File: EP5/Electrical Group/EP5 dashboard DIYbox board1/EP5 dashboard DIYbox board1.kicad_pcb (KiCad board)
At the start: 2 copper layers, 138.2 x 72.5 mm, 161 parts, among them J1 pedal2-2, J10 12864, J11 pedal1-1, J12 pedal1-2, J14 screen, J2 pedal2-1, J4 R1, J5 L1, J6 L2, J7 L3, J8 L4, J9 RTD, U1 Seg1, U10 74HC595, U11 74HC595, U12 74HC595, U13 74HC595, U14 74HC595, U15 74HC595, U16 74HC595, U17 74HC595, U2 Seg2, U5 Seg3, U6 Seg4, U7 74HC595, U8 74HC595, U9 74HC595

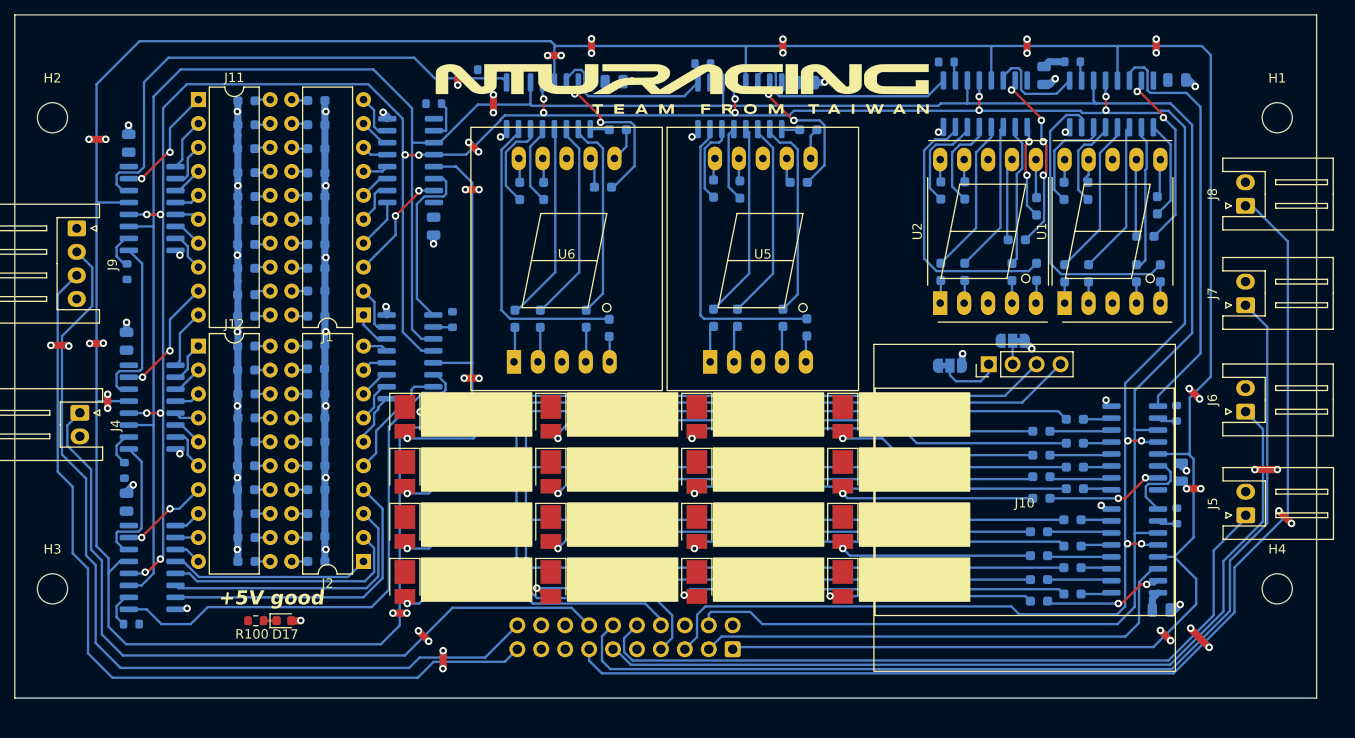
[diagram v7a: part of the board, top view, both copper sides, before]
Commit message: update dashboard 1 to V2.3 in EP5
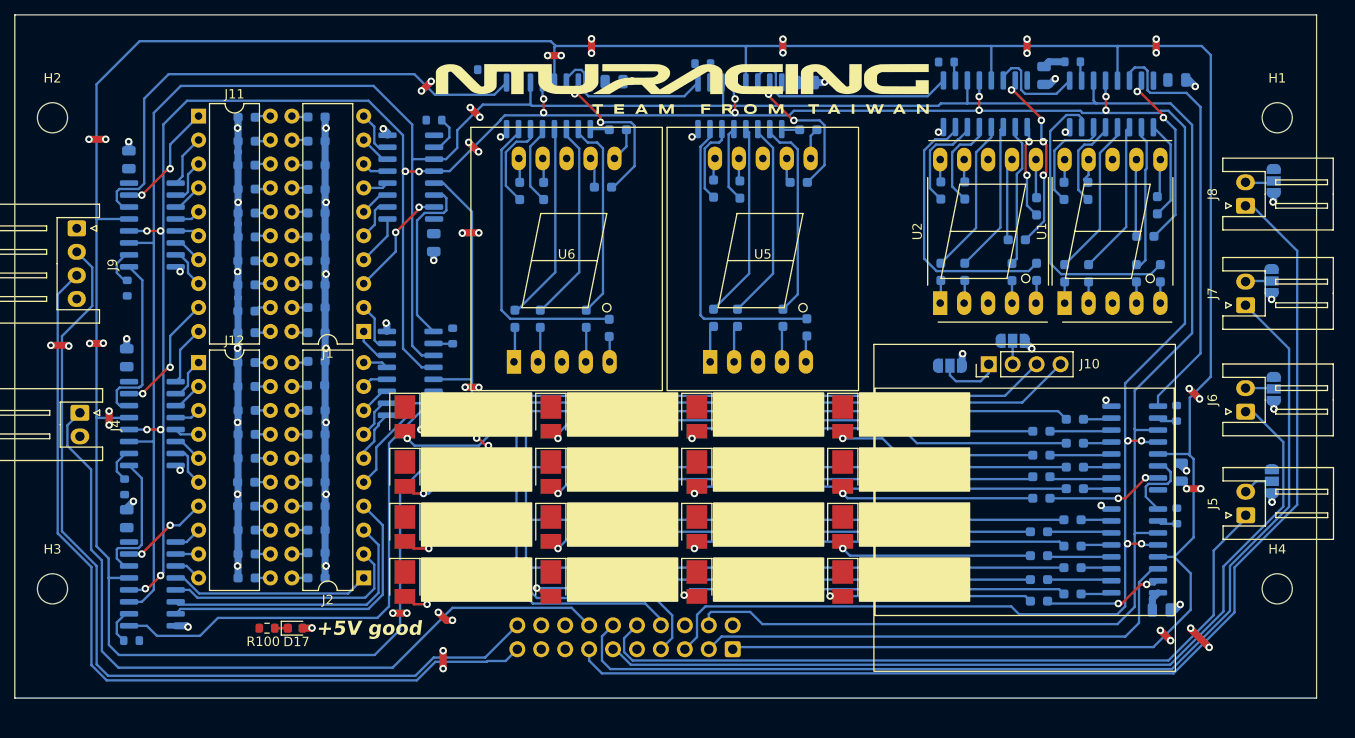
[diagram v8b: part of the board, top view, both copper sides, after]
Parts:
- added JP3: OLED_P1, Jumper:SolderJumper-3_P1.3mm_Open_RoundedPad1.0x1.5mm, B.Cu at (201.0, 94.2)
- added JP4: OLED_P1, Jumper:SolderJumper-3_P1.3mm_Open_RoundedPad1.0x1.5mm, B.Cu at (201.2, 84.4)
- added JP5: OLED_P1, Jumper:SolderJumper-3_P1.3mm_Open_RoundedPad1.0x1.5mm, B.Cu at (201.0, 73.0)
- added JP6: OLED_P1, Jumper:SolderJumper-3_P1.3mm_Open_RoundedPad1.0x1.5mm, B.Cu at (201.2, 62.3)
- C1, C10, C11, C2, C3, C4, C5, C6, C7, C8, C9: value 0u1 16V -> 0u1
- D17: value 5VGood -> White 5VGood
- J1: value pedal2-2 -> pedal2-2 GREEN
- J11: value pedal1-1 -> pedal1-1 RED
- J12: value pedal1-2 -> pedal1-2 RED
- J2: value pedal2-1 -> pedal2-1 GREEN
- JP1, JP2: footprint Jumper:SolderJumper-3_P1.3mm_Bridged12_RoundedPad1.0x1.5mm -> Jumper:SolderJumper-3_P1.3mm_Open_RoundedPad1.0x1.5mm
- R1, R10, R11, R12, R13, R14, R15, R16, R2, R3, R4, R5, R6, R7, R8, R9: value 220 -> 390R
- R100: value 220R -> 510R
- R17, R18, R19, R20, R21, R22, R23, R24, R25, R26, R27, R28, R29, R30, R31, R32: value 220 -> 180R
- R33, R34, R35, R36, R37, R38, R39, R40, R41, R42, R43, R44, R45, R46, R47, R48, R77, R78, R79, R80, R81, R82, R83, R84, R85, R86, R87, R88, R89, R90, R91, R92, R93, R94, R95, R96: value 220 -> 220R
- R49, R50, R51, R52, R53, R54, R55, R56, R57, R58, R59, R60, R61, R62, R63, R64, R65, R66, R67, R68: value 220 -> 330R
- R69, R70, R71, R72, R73, R74, R75, R76, R97, R98, R99: value 1k -> 10k
- U1: value Seg1 -> Seg1 GREEN .56
- U2: value Seg2 -> Seg2 GREEN .56
- U5: value Seg3 -> Seg3 BLUE .8
- U6: value Seg4 -> Seg4 BLUE .8
- moved C2 1.75 mm to (79.4, 81.1)
- moved C5 1.75 mm to (112.0, 68.9)
- moved J12 1.75 mm to (87.1, 81.6)
- moved J2 1.75 mm to (104.6, 104.5)
- moved R49 1.75 mm to (99.6, 101.8)
- moved R52 1.75 mm to (99.6, 104.5)
- moved R56 1.75 mm to (99.6, 91.8)
- moved R58 1.75 mm to (99.6, 86.7)
- moved R59 1.75 mm to (99.5, 84.0)
- moved R62 1.75 mm to (99.6, 70.8)
- moved R64 1.75 mm to (99.6, 65.7)
- moved R81 1.75 mm to (92.2, 65.7)
- moved R83 1.75 mm to (92.2, 70.8)
- moved R87 1.75 mm to (92.2, 81.6)
- moved R89 1.75 mm to (92.2, 86.7)
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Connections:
- J5 pad 2: GND -> Net-(J5-Pin_2)
- J6 pad 2: GND -> Net-(J6-Pin_2)
- J7 pad 2: GND -> Net-(J7-Pin_2)
- J8 pad 2: GND -> Net-(J8-Pin_2)
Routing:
- net +5V: track 46.1 -> 39.8 mm, vias 47 -> 43
- net GND: track 115.4 -> 120.1 mm, vias 38 -> 42
- net Net-(J5-Pin_2): track 0.00 -> 3.23 mm
- net Net-(J8-Pin_2): track 0.00 -> 3.11 mm
- net Net-(J6-Pin_2): track 0.00 -> 3.03 mm
- net Net-(J7-Pin_2): track 0.00 -> 2.79 mm
- net ButtonR2_raw: track 91.5 -> 93.8 mm
- net ButtonL1_raw: track 81.1 -> 83.2 mm
- net ButtonRTDlight: track 92.7 -> 94.7 mm
- net ButtonR3_raw: track 108.9 -> 110.8 mm
- net SRCLK: track 317.5 -> 319.3 mm
- net ButtonR4_raw: track 120.7 -> 121.5 mm
- net ButtonRTD_raw: track 90.2 -> 90.9 mm
- net RCLK: track 322.6 -> 323.3 mm
- net Net-(D16-A): track 72.5 -> 73.2 mm
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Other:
- board text added: "EP5 V2.3 dashboard 1 Jack Kuo 2024/08/28"
- board text removed: "EP5 V2.2 dashboard 1 Jack Kuo"
